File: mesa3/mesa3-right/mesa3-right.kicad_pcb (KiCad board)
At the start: 2 copper layers, 214 x 111 mm, 55 parts, among them J2 Tag-Connect TC2030

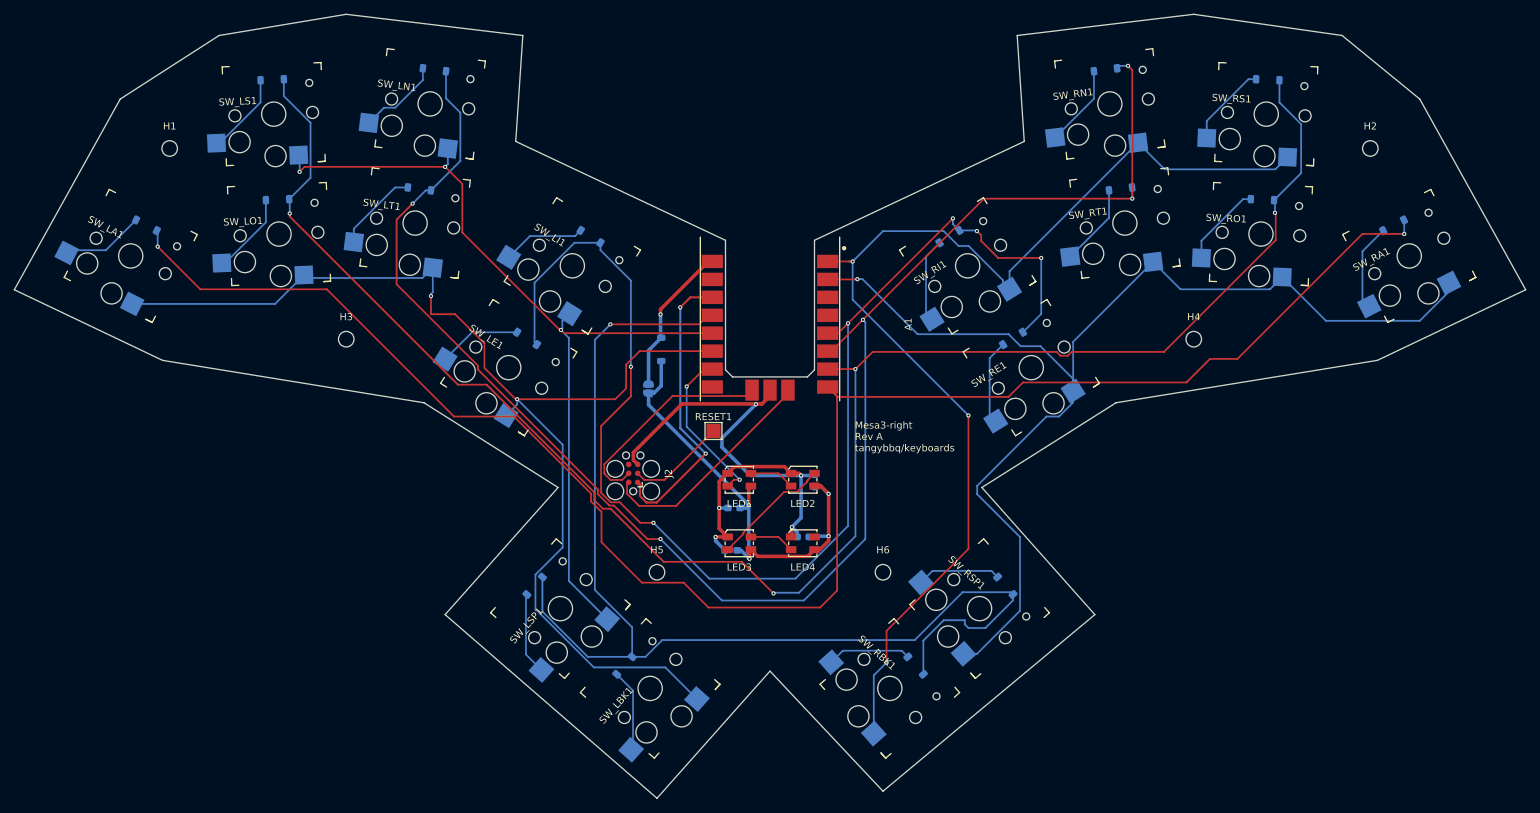
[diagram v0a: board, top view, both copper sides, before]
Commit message: Split the Mesa 3 into left and right halves
Each half now carries its own nine keys, its own outline and its own
routing. The left keeps the Tiny2040, the LEDs, the Tag-Connect and the
reset pad; the right is switches, diodes and the RJ-45 and nothing else,
with no power and no ground anywhere on it.

The two checks that mattered both hold. The RJ-45 pinout is identical at
both ends, so a straight-through cable is correct -- the pin order runs
opposite between the halves, which is what a part that cannot be mirrored
does, and does not matter since the nets match. And all eighteen keys
keep their exact mesa2 column and row, so one keymap still serves Rev B
and both halves.

Record the review findings as accepted rather than outstanding, and
correct LAYOUT.md: the unconnected GND that DRC reports is a false
positive. The symbol ties the module's ground pads into one net, so DRC
wants copper between them, but the module commons them internally and
the board does not need to.

Assisted-by: Claude:opus-5
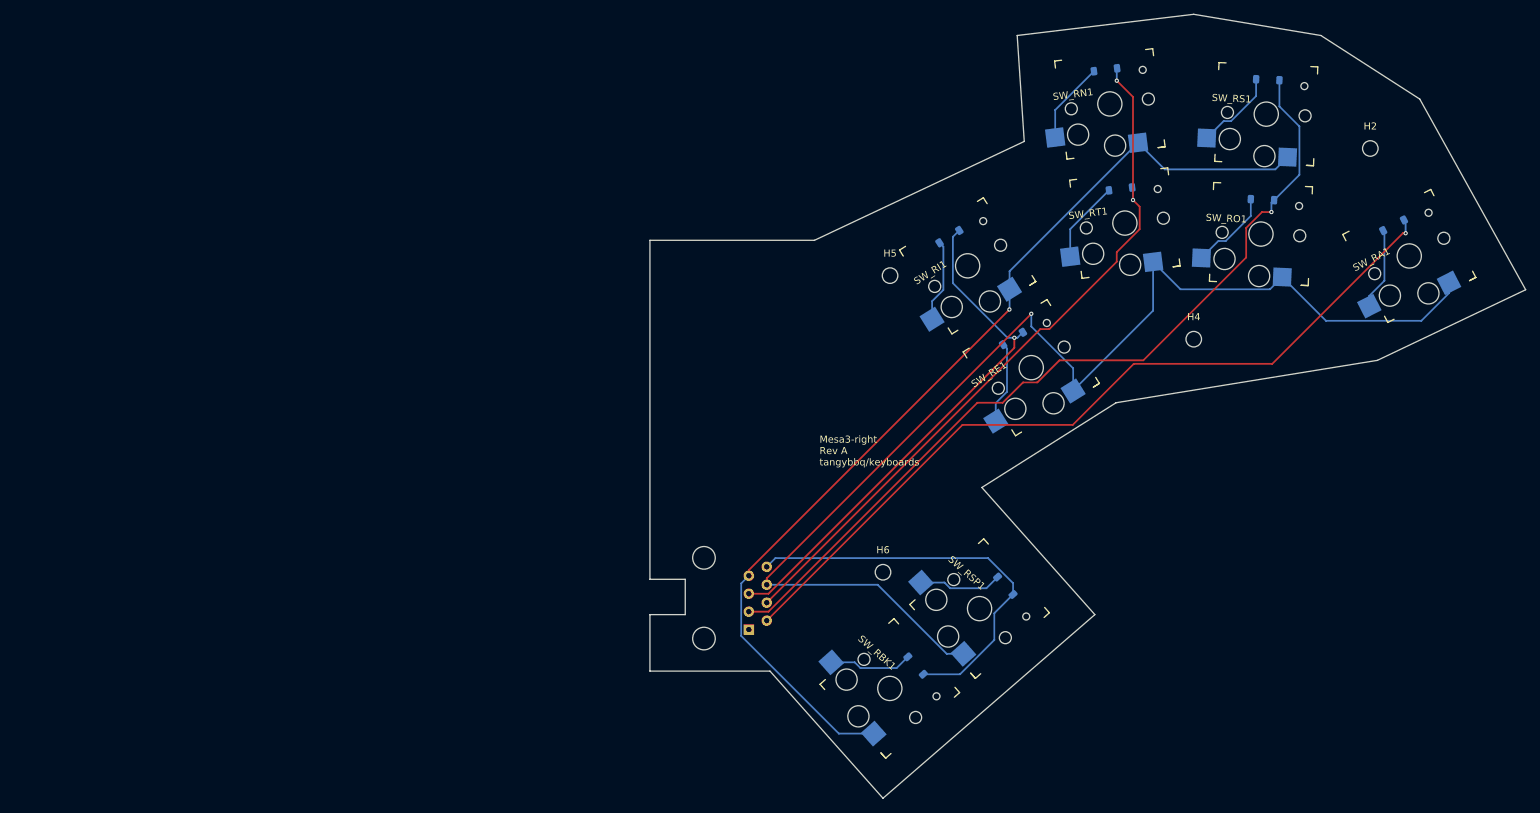
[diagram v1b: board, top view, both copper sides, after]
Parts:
- removed A1: Pimoroni_Tiny2040, mesa1:Pimoroni_Tiny2040
- removed C1, C2, C3, C4: 100nF, Capacitor_SMD:C_0603_1608Metric_Pad1.08x0.95mm_HandSolder
- removed D1, D_LA1, D_LBK1, D_LE1, D_LI1, D_LN1, D_LO1, D_LS1, D_LSP1, D_LT1: 1N4148W, Diode_SMD:D_SOD-123
- removed H1, H3: MountingHole, MountingHole:MountingHole_2.2mm_M2
- removed J2: Tag-Connect TC2030, Connector:Tag-Connect_TC2030-IDC-FP_2x03_P1.27mm_Vertical
- removed JP1: SolderJumper_2_Open, Jumper:SolderJumper-2_P1.3mm_Open_RoundedPad1.0x1.5mm
- removed LED1, LED2, LED3, LED4: SK6812MINI-HS, mesa1:SK6812-MINI-HS
- removed RESET1: RESET_WIRE, TestPoint:TestPoint_Pad_2.0x2.0mm
- removed SW_LA1, SW_LBK1, SW_LE1, SW_LI1, SW_LN1, SW_LO1, SW_LS1, SW_LSP1, SW_LT1: SW_PG1350, mesa1:Kailh_socket_PG1350
- added J1: RJ45, Connector_RJ:RJ45_Amphenol_54602-x08_Horizontal, B.Cu at (132.0, 113.1)
- moved H5 53.4 mm to (152.0, 63.0)
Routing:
- net /ROW_B: track 168.4 -> 0.00 mm, vias 2 -> 0
- net /COL_1: track 247.0 -> 115.2 mm, vias 2 -> 1
- net /COL_3: track 230.0 -> 101.5 mm, vias 5 -> 2
- net /COL_2: track 249.2 -> 121.4 mm, vias 4 -> 1
- net /ROW_A: track 124.1 -> 0.00 mm, vias 3 -> 0
- net /COL_4: track 183.1 -> 74.7 mm, vias 6 -> 1
- net /COL_5: track 165.2 -> 58.1 mm, vias 1 -> 0
- net /GND: track 86.0 -> 0.00 mm, vias 5 -> 0
- net /+4V5: track 70.1 -> 0.00 mm, vias 4 -> 0
- net /+3V3: track 41.9 -> 0.00 mm, vias 2 -> 0
- net /SWDIO: track 32.3 -> 0.00 mm
- net /SWCLK: track 30.8 -> 0.00 mm
- net /RGB: track 23.1 -> 0.00 mm, vias 2 -> 0
- net /+5V: track 21.5 -> 0.00 mm, vias 1 -> 0
- net /ROW_C: track 162.1 -> 141.1 mm, vias 3 -> 1
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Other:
- board size 214 x 111 mm -> 124 x 111 mm

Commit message: Bump both mesa3 halves to Rev B
Rev A of both halves has gone to the fab and the boards are on their way
here, so by the rule in mesa3-tasks.md the letter moves on before any
further change is made to the designs.  This commit is the bump alone and
touches no geometry, netlist or routing.

Each half carries the revision in three places, all updated together: the
PCB and schematic title blocks, and sch_revision in the project file.  The
silkscreen legend that the bare board is identified by moves with them, so
the delivered Rev A boards stay distinguishable from whatever Rev B
becomes.

KiCad also reordered used_designators in mesa3-right.kicad_pro while
saving; the set is unchanged.
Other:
- board text added: "Mesa3-right Rev B tangybbq/keyboards"
- board text removed: "Mesa3-right Rev A tangybbq/keyboards"
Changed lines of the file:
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@@
 		(title "mesa3-right")
 		(date "2026-08-09")
-		(rev "A")
+		(rev "B")
 	)
 	(layers
@@
 		(layer "Edge.Cuts")
 	)
-	(gr_text "Mesa3-right\nRev A\ntangybbq/keyboards"
+	(gr_text "Mesa3-right\nRev B\ntangybbq/keyboards"
 		(at 142 90 0)
 		(layer "F.SilkS")

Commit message: Route both mesa3 halves and finish the right FN key
Rev B is now routed on both hands.  The left half went from bare
placement to 337 segments and 36 vias; the right went from 118 segments
and 7 vias to 149 and 9 as the mode key was wired in.  That key was the
last thing outstanding — on the right the switch and diode were on the
board but deliberately left disconnected, and they now sit at
COL_1/ROW_C, one of the two slots the dropped outer pinky freed,
matching COL_1/ROW_A on the left.  Each half therefore gains one Kailh
socket and one 1N4148W over Rev A.

fnkey.py now places both halves instead of only the left, as its own
docstring said it should when the right-hand key was still undecided.
Each FN key is derived from its own anchor — a local (PITCH, 0) offset
in SW_xE1's frame, carrying that switch's rotation — and the sign flips
on the right, where local +X points outboard rather than inboard.
Because the two halves are computed independently, their mirror
symmetry is a genuine cross-check rather than a restatement of the same
arithmetic, so the script now makes it one: it refuses to write unless
every switch and diode pair sums to 270.0 mm in x, shares a y, and has
opposite rotations.  The hand placement this replaced was 0.846 mm out;
the new keycap clears SW_RE1 by the 0.500 mm target exactly.

apply-fnkey.py follows, walking both boards from a board-keyed
fn-placement.json and saving only the ones that actually moved.  It
still goes through pcbnew rather than Konnect's IPC path, which
continues to segfault KiCAD 10.0.5 on this machine.

Assisted-by: Claude:opus-5
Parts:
- added D_RFN1: 1N4148W, Diode_SMD:D_SOD-123, B.Cu at (154.1, 81.4)
- added SW_RFN1: SW_PG1350, mesa1:Kailh_socket_PG1350, F.Cu at (156.7, 85.6)
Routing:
- net /ROW_C: track 141.1 -> 158.3 mm, vias 1 -> 2
- net Net-(D_RFN1-A): track 0.00 -> 12.0 mm
- net /COL_1: track 115.2 -> 126.7 mm, vias 1 -> 2
- net /COL_3: track 101.5 -> 103.5 mm
- net /COL_2: track 121.4 -> 119.8 mm
- net /ROW_D: track 172.0 -> 173.3 mm
- net /COL_4: track 74.7 -> 76.0 mm
